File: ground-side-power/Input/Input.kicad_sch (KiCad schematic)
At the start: 37 parts, among them J1 Battery Terminals, J2 Battery Terminals, J26 Conn_01x02_Female, J3 Battery Terminals, J4 Battery Terminals, J5 455860005, J6 455860005, J7 ATX-24, J8 Conn_01x03_Female, J9 Conn_01x03_Female, K1 AZ2150-1A-12DEF, M1 Fan_PC_Chassis, SW1 GRB234A2NABA1, U1 INA180, U2 INA180

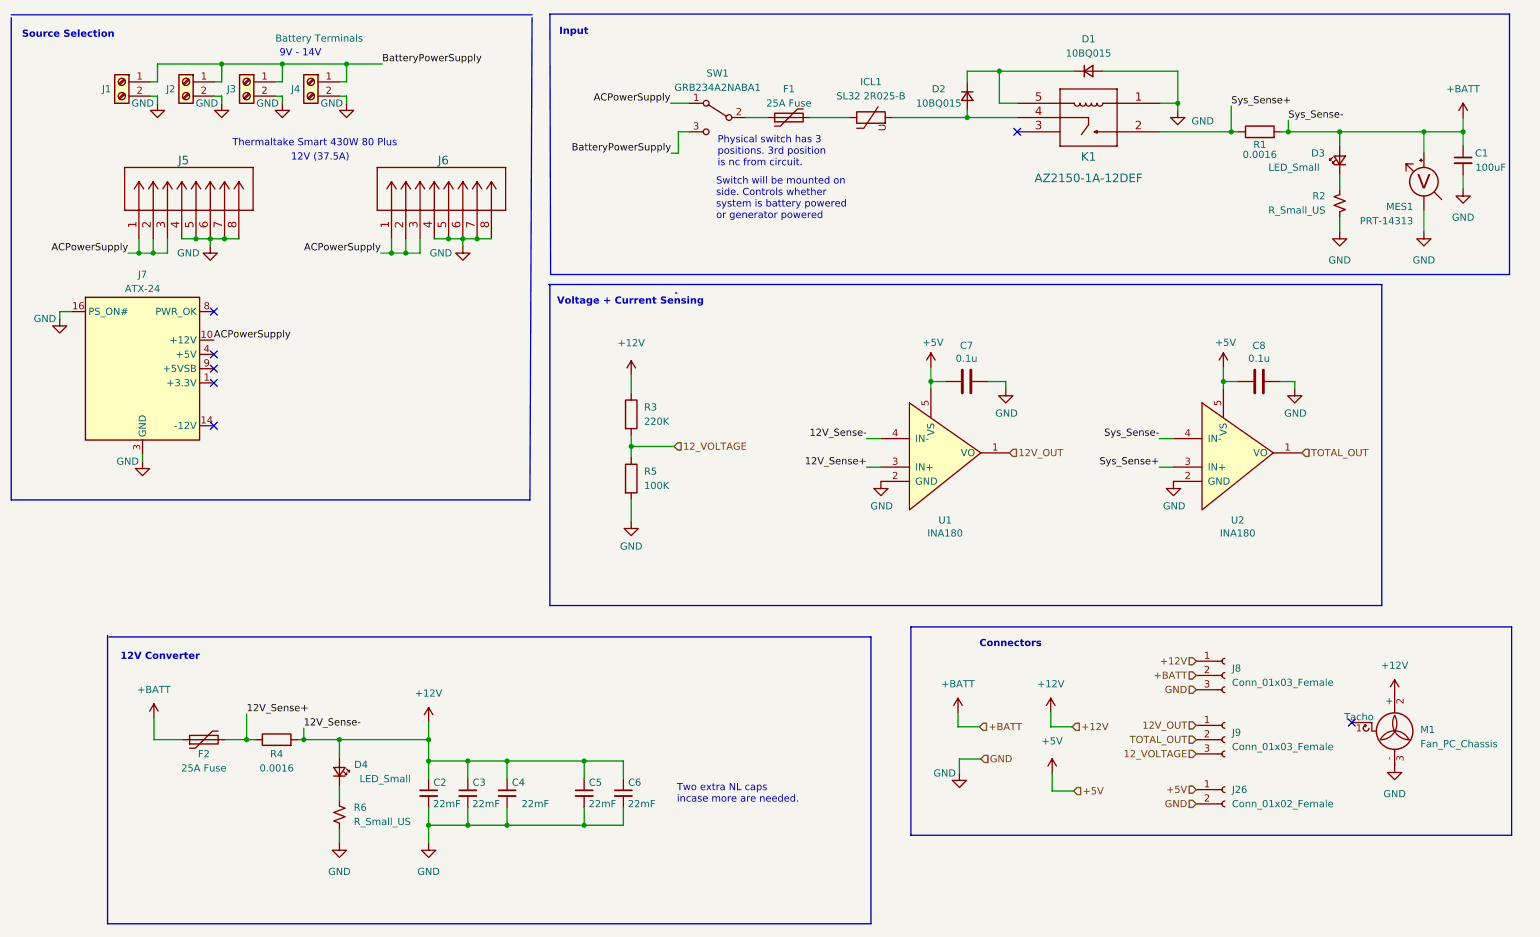
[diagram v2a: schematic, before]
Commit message: Address Input and Converter Comments
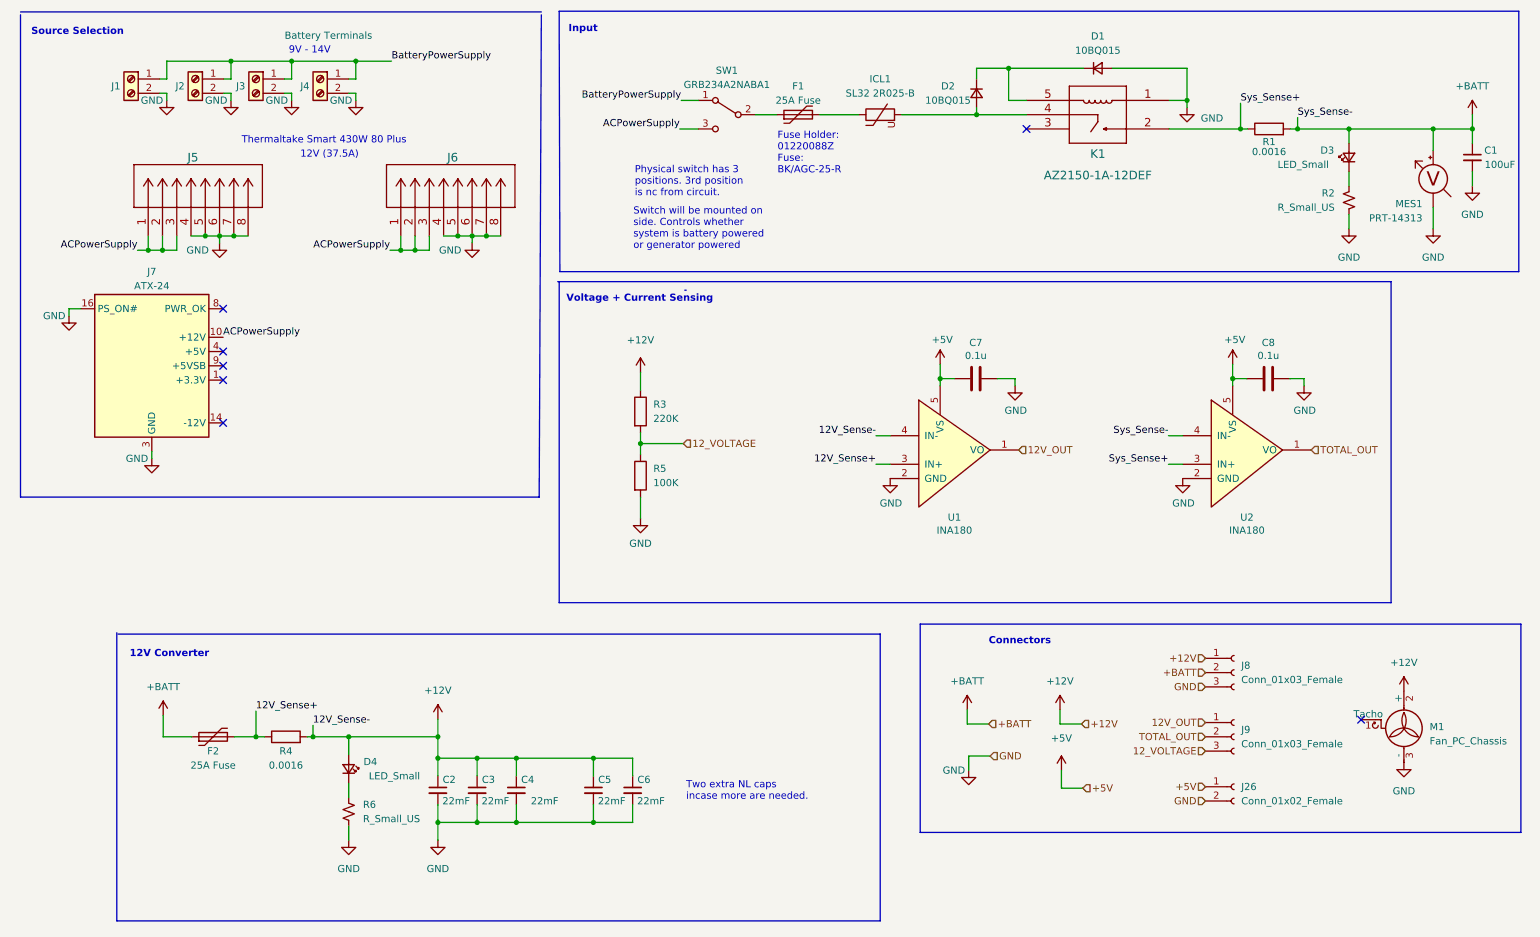
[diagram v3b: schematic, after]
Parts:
- C1: footprint Capacitor_SMD:C_1206_3216Metric_Pad1.33x1.80mm_HandSolder -> Capacitor_THT:CP_Radial_D6.3mm_P2.50mm
- D1: footprint Capacitor_SMD:C_0603_1608Metric_Pad1.08x0.95mm_HandSolder -> Diode_SMD:D_SMB_Handsoldering
- D2: footprint Diode_SMD:D_SMB -> Diode_SMD:D_SMB_Handsoldering
- D3, D4: footprint Diode_SMD:D_0805_2012Metric -> Diode_SMD:D_1206_3216Metric_Pad1.42x1.75mm_HandSolder
- F1, F2: footprint Fuse:Fuse_1206_3216Metric_Pad1.42x1.75mm_HandSolder -> Fuse:Fuseholder_Clip-6.3x32mm_Littelfuse_102_122_Inline_P34.21x7.62mm_D1.98mm_Horizontal
- J1, J2, J26, J3, J4: footprint GSP:OSTTA020161 -> GSP:1935310
- J8, J9, SW1: footprint GSP:TB005-762-03BE -> GSP:1935323
- R2, R6: footprint Resistor_SMD:R_1206_3216Metric_Pad1.30x1.75mm_HandSolder -> Resistor_SMD:R_0805_2012Metric_Pad1.20x1.40mm_HandSolder
- R3, R5: footprint Resistor_SMD:R_0402_1005Metric_Pad0.72x0.64mm_HandSolder -> Resistor_SMD:R_0805_2012Metric_Pad1.20x1.40mm_HandSolder
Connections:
- net ACPowerSupply: now also SW1.3 (C); no longer SW1.1 (A)
- net BatteryPowerSupply: now also SW1.1 (A); no longer SW1.3 (C)
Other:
- note added: "Fuse Holder: 01220088Z Fuse: BK/AGC-25-R"

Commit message: Resolved Final Issues
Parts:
- removed C5, C6: 22mF, GSP:LLS1C223MELZ, symbol Device:C_Small
- added R17: 10k, symbol Device:R_Small_US
- J5, J6: value 455860005 -> 874270842; footprint GSP:MOLEX_455860005 -> GSP:MOLEX_874270842
- J7: footprint GSP:MOLEX_15246240 -> GSP:MOLEX_442060001
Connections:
- net +12V: now also R17.1
- net GND: now also R17.2

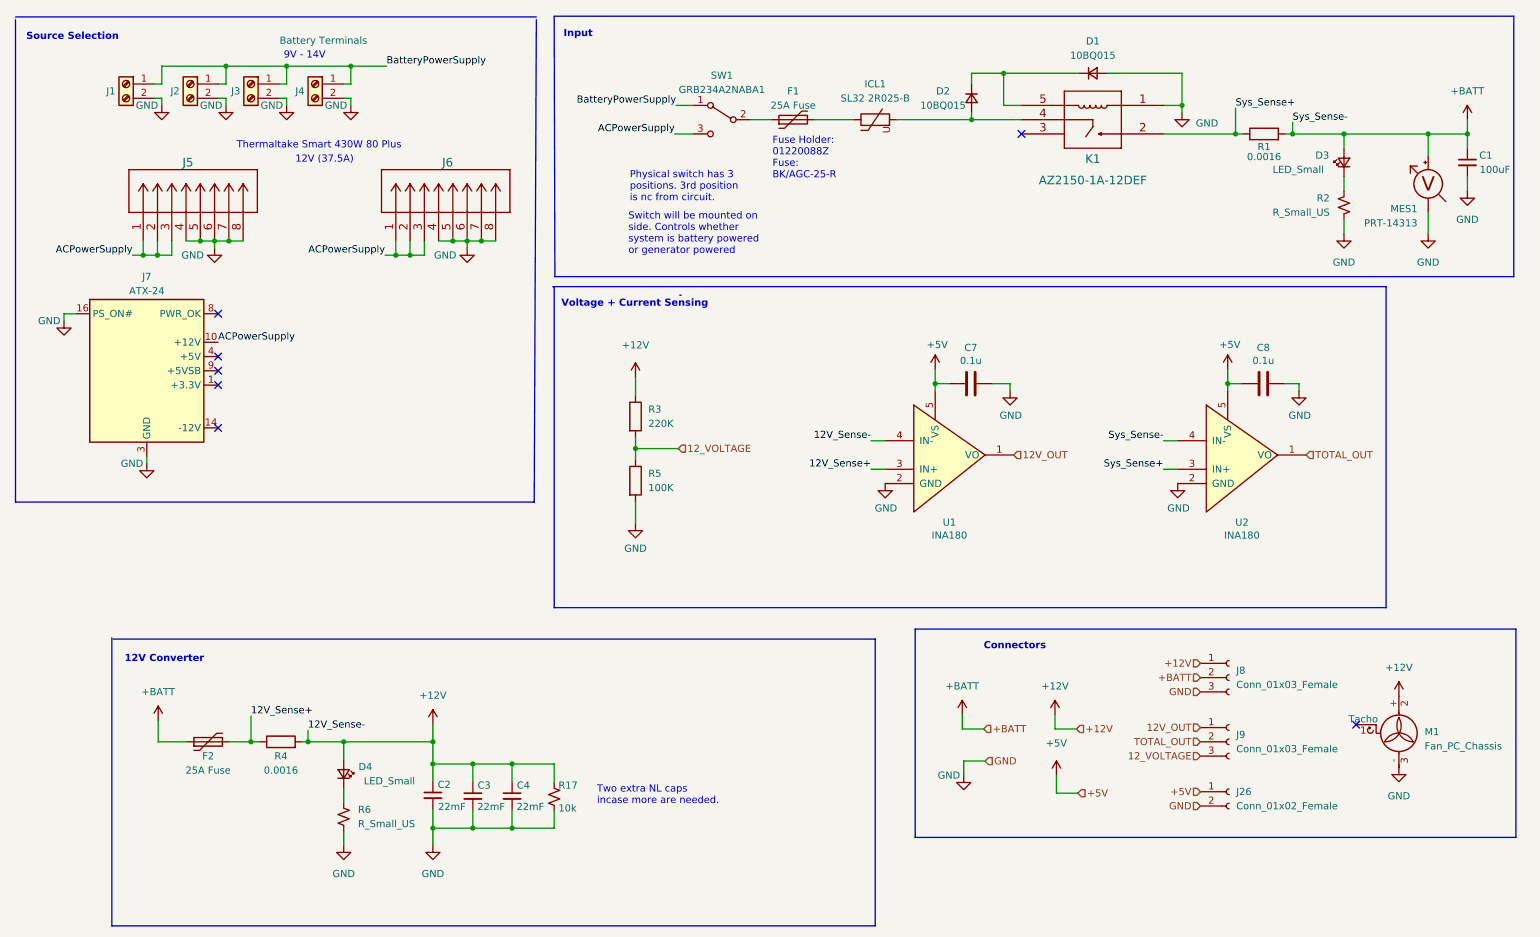
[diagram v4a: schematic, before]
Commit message: Silkscreen and current sense changes
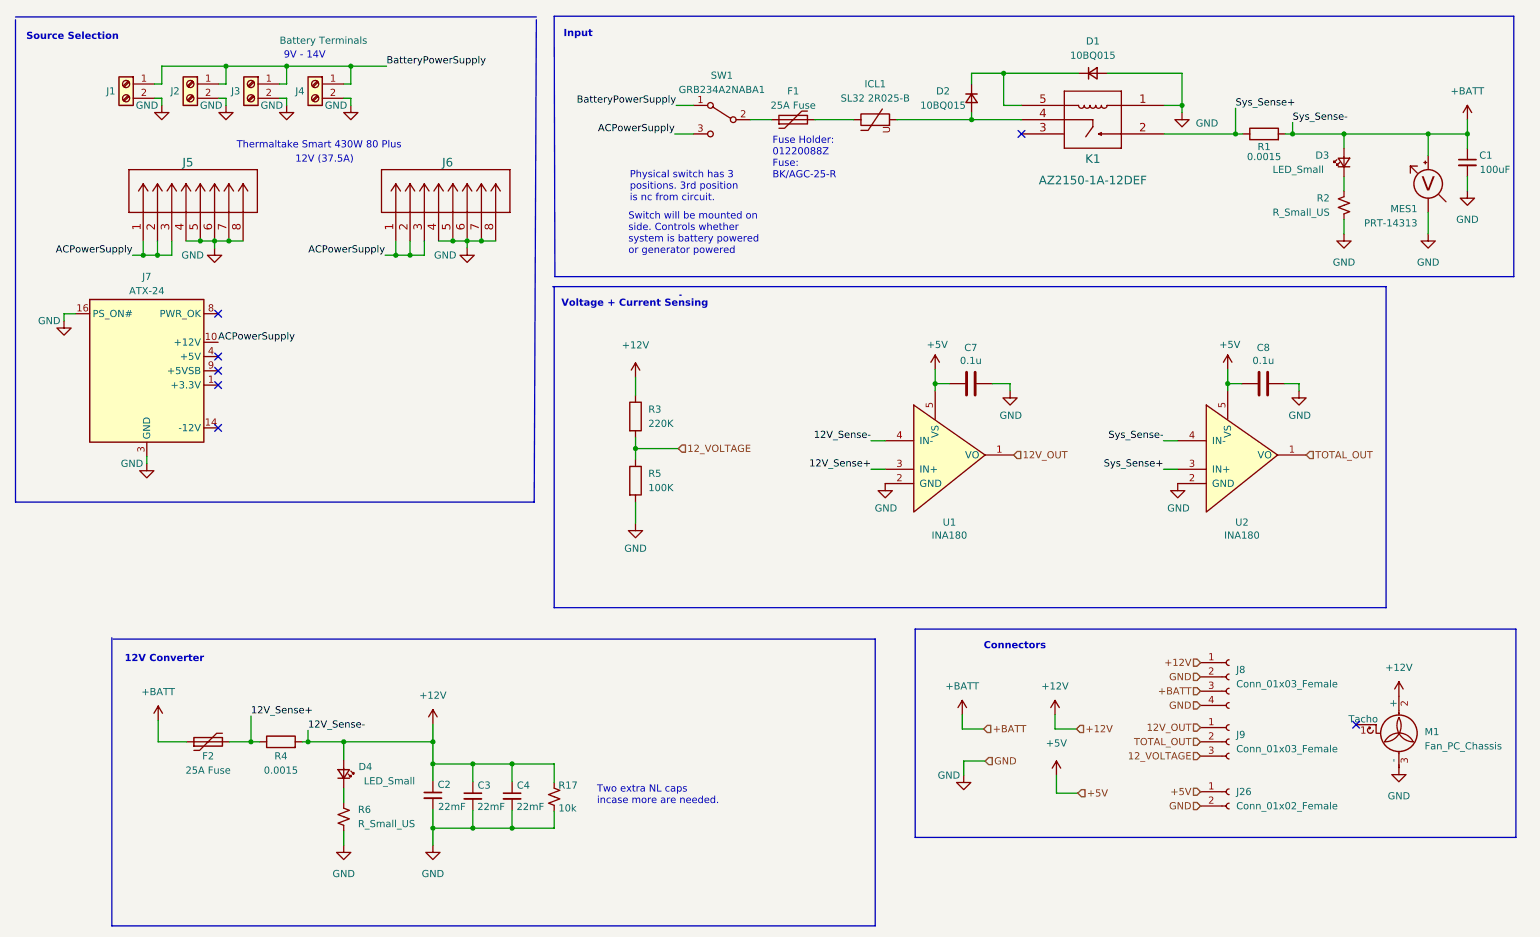
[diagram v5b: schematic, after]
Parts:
- J8: footprint GSP:1935323 -> GSP:CUI_TB008A-508-04BE; symbol Connector:Conn_01x03_Female -> Connector:Conn_01x04_Female
- R1, R4: value 0.0016 -> 0.0015; footprint Resistor_SMD:R_1206_3216Metric_Pad1.30x1.75mm_HandSolder -> Resistor_SMD:R_2512_6332Metric_Pad1.40x3.35mm_HandSolder
- R17: footprint (none) -> Resistor_SMD:R_0805_2012Metric_Pad1.20x1.40mm_HandSolder
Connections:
- net +BATT: now also J8.3 (Pin_3); no longer J8.2 (Pin_2)
- net GND: now also J8.2 (Pin_2), J8.4 (Pin_4); no longer J8.3 (Pin_3)
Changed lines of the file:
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@@
     (effects (font (size 1.27 1.27)) (justify left))
   )
-  (hierarchical_label "+BATT" (shape input) (at 226.06 134.747 180)
+  (hierarchical_label "+BATT" (shape input) (at 226.06 137.16 180)
+    (effects (font (size 1.27 1.27)) (justify right))
+  )
+  (hierarchical_label "GND" (shape input) (at 226.06 134.62 180)
     (effects (font (size 1.27 1.27)) (justify right))
   )
@@
     (effects (font (size 1.27 1.27)) (justify right))
   )
-  (hierarchical_label "+12V" (shape input) (at 226.06 132.207 180)
+  (hierarchical_label "+12V" (shape input) (at 226.06 132.08 180)
     (effects (font (size 1.27 1.27)) (justify right))
   )
@@
     (effects (font (size 1.27 1.27)) (justify left))
   )
-  (hierarchical_label "GND" (shape input) (at 226.06 137.287 180)
+  (hierarchical_label "GND" (shape input) (at 226.06 139.7 180)
     (effects (font (size 1.27 1.27)) (justify right))
   )
@@
     (in_bom yes) (on_board yes)
     (property "Reference" "R1" (id 0) (at 237.363 40.259 90))
-    (property "Value" "0.0016" (id 1) (at 237.363 42.037 90))
-    (property "Footprint" "Resistor_SMD:R_1206_3216Metric_Pad1.30x1.75mm_HandSolder" (id 2) (at 237.363 39.751 90)
+    (property "Value" "0.0015" (id 1) (at 237.363 42.037 90))
+    (property "Footprint" "Resistor_SMD:R_2512_6332Metric_Pad1.40x3.35mm_HandSolder" (id 2) (at 237.363 39.751 90)
       (effects (font (size 1.27 1.27)) hide)
     )
@@
     (in_bom yes) (on_board yes)
     (property "Reference" "R4" (id 0) (at 62.357 148.717 90))
-    (property "Value" "0.0016" (id 1) (at 62.357 151.257 90))
-    (property "Footprint" "Resistor_SMD:R_1206_3216Metric_Pad1.30x1.75mm_HandSolder" (id 2) (at 62.357 147.955 90)
+    (property "Value" "0.0015" (id 1) (at 62.357 151.257 90))
+    (property "Footprint" "Resistor_SMD:R_2512_6332Metric_Pad1.40x3.35mm_HandSolder" (id 2) (at 62.357 147.955 90)
       (effects (font (size 1.27 1.27)) hide)
     )
@@
       (effects (font (size 1.27 1.27)) (justify left))
     )
-    (property "Footprint" "" (id 2) (at 110.998 155.956 0)
+    (property "Footprint" "Resistor_SMD:R_0805_2012Metric_Pad1.20x1.40mm_HandSolder" (id 2) (at 110.998 155.956 0)
       (effects (font (size 1.27 1.27)) hide)
     )
@@
     (pin "2")
   )
-  (symbol (lib_id "Connector:Conn_01x03_Female") (at 231.14 134.747 0) (unit 1)
-    (in_bom yes) (on_board yes) (fields_autoplaced)
-    (property "Reference" "J8" (id 0) (at 232.41 133.4769 0)
-      (effects (font (size 1.27 1.27)) (justify left))
-    )
-    (property "Value" "Conn_01x03_Female" (id 1) (at 232.41 136.0169 0)
-      (effects (font (size 1.27 1.27)) (justify left))
-    )
-    (property "Footprint" "GSP:1935323" (id 2) (at 231.14 134.747 0)
-      (effects (font (size 1.27 1.27)) hide)
-    )
-    (property "Datasheet" "~" (id 3) (at 231.14 134.747 0)
+  (symbol (lib_id "Connector:Conn_01x04_Female") (at 231.14 134.62 0) (unit 1)
+    (in_bom yes) (on_board yes) (fields_autoplaced)
+    (property "Reference" "J8" (id 0) (at 232.41 133.3499 0)
+      (effects (font (size 1.27 1.27)) (justify left))
+    )
+    (property "Value" "Conn_01x03_Female" (id 1) (at 232.41 135.8899 0)
+      (effects (font (size 1.27 1.27)) (justify left))
+    )
+    (property "Footprint" "GSP:CUI_TB008A-508-04BE" (id 2) (at 231.14 134.62 0)
+      (effects (font (size 1.27 1.27)) hide)
+    )
+    (property "Datasheet" "~" (id 3) (at 231.14 134.62 0)
       (effects (font (size 1.27 1.27)) hide)
     )
@@
     (pin "2")
     (pin "3")
+    (pin "4")
   )
   (symbol (lib_id "power:GND") (at 63.373 32.893 0) (mirror y) (unit 1)
@@
     )
     (path "/b508d950-d944-419d-b092-dcb7158383f5"
-      (reference "J8") (unit 1) (value "Conn_01x03_Female") (footprint "GSP:1935323")
+      (reference "J8") (unit 1) (value "Conn_01x03_Female") (footprint "GSP:CUI_TB008A-508-04BE")
     )
     (path "/4b6fcc0d-9de6-420e-ab0c-42b7c6e55fc3"
